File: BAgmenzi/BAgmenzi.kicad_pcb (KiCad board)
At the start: 6 copper layers, 140 parts, among them IC1 TPL0501-100RSER, J2 DF52-2S-0.8H(21), J3 USB3076-30-A, M1 *, Q1 NX7002BKMBYL, U1 MSP430FR5043IRGCT, U10 PESD1USB30, U11 MAX77654BENV+T, U12 TS5A3159AYZPR, U13 TPS7A2033DBVDQN, U14 TPS63900, U2 AD8338ACPZ-R7, U3 OPA836IDBVT, U4 OPA836IDBVT, U7 LT3463AEDD#PBF, U8 TPS22916CYFPR, U9 MAXM86161EFD_T, X1 FY0800018, X2 ABS07-32.768KHZ-9-T, Y1 AWSCR-8.00CV-T

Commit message: started layout, front v backside
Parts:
- removed C55: 0.1u, Capacitor_SMD:C_0402_1005Metric
- removed C56: 10u, Capacitor_SMD:C_0402_1005Metric
- removed C57: 22u, Capacitor_SMD:C_0402_1005Metric
- removed D1: APHD1608LZGCK, wulpus:FP-APHD1608LZGCK-MFG
- removed L8: 2.2uH, Inductor_SMD:L_Murata_DFE201610P
- removed R37: 100k, Resistor_SMD:R_0402_1005Metric
- removed R38: 20.5k, Resistor_SMD:R_0402_1005Metric
- removed R39, R40: 0, Resistor_SMD:R_0402_1005Metric
- removed R6: 22, Resistor_SMD:R_0402_1005Metric
- removed U12: TS5A3159AYZPR, wulpus_pro_acq:BGA6C50P2X3_89X139X50
- removed U14: TPS63900, Package_SON:WSON-10-1EP_2.5x2.5mm_P0.5mm_EP1.2x2mm_ThermalVias
- added C61: 2.2U 50v, EEG_PcbLib:0402, F.Cu at (149.6, 117.5)
- added C62: 2.2U 50v, EEG_PcbLib:0402, F.Cu at (165.4, 141.2)
- added J1: Conn_01x07, Connector_PinHeader_2.54mm:PinHeader_1x07_P2.54mm_Vertical, F.Cu at (74.3, 168.0)
- added J4: connector for CMUT, cmut_dummy:cmut-dummy, F.Cu at (159.9, 128.7)
- added J5: 3220-10-0100-00, EEG_PcbLib:CONN_3220-10-0100-00_CNC, F.Cu at (35.2, 166.0)
- added JP1: SolderJumper_3_Open, Jumper:SolderJumper-3_P1.3mm_Open_Pad1.0x1.5mm, F.Cu at (146.7, 141.7)
- added JP2: SolderJumper_3_Open, Jumper:SolderJumper-3_P1.3mm_Open_Pad1.0x1.5mm, F.Cu at (149.4, 110.5)
- added JP3: SolderJumper_3_Open, Jumper:SolderJumper-3_P1.3mm_Open_Pad1.0x1.5mm, F.Cu at (146.7, 137.9)
- added JP4: SolderJumper_3_Open, Jumper:SolderJumper-3_P1.3mm_Open_Pad1.0x1.5mm, F.Cu at (149.4, 115.2)
- added JP5: SolderJumper_3_Open, Jumper:SolderJumper-3_P1.3mm_Open_Pad1.0x1.5mm, F.Cu at (165.1, 138.7)
- added JP7: SolderJumper_3_Open, Jumper:SolderJumper-3_P1.3mm_Open_Pad1.0x1.5mm, F.Cu at (37.4, 112.6)
- added R41: 100K, Resistor_SMD:R_0402_1005Metric, F.Cu at (150.0, 112.3)
- added R42: 100K, Resistor_SMD:R_0402_1005Metric, F.Cu at (146.6, 135.4)
- added R43: 100K, EEG_PcbLib:0402, F.Cu at (149.6, 118.7)
- added R44: 30k, EEG_PcbLib:0402, F.Cu at (163.6, 141.0)
- C33: footprint Capacitor_SMD:C_0201_0603Metric -> Capacitor_SMD:C_0402_1005Metric
- C59: value 1u -> 2.2u
- C63: footprint Capacitor_SMD:C_0201_0603Metric -> EEG_PcbLib:0402
- TP2: footprint TestPoint:TestPoint_Loop_D2.50mm_Drill1.85mm -> TestPoint:TestPoint_Pad_D2.0mm
- TP6: footprint TestPoint:TestPoint_Loop_D2.50mm_Drill1.0mm_LowProfile -> TestPoint:TestPoint_Pad_D2.0mm
- TP7: footprint EEG_PcbLib:TEST_POINT_KEYSTONE_5007_TRAD -> TestPoint:TestPoint_THTPad_1.0x1.0mm_Drill0.5mm
- moved L6 220.9 mm to (41.8, 140.3)
- moved R21 220.0 mm to (46.0, 137.1)
- moved R22 220.0 mm to (48.5, 139.9)
- moved R25 220.0 mm to (44.9, 142.3)
- moved C39 220.0 mm to (41.7, 139.2)
- moved C40 220.0 mm to (44.3, 137.2)
- moved C43 220.0 mm to (50.0, 141.4)
- moved D2 220.0 mm to (47.5, 142.4)
- moved L5 220.0 mm to (42.6, 138.1)
- moved R20 220.0 mm to (46.0, 136.1)
- moved R23 220.0 mm to (48.5, 140.9)
- moved R24 220.0 mm to (43.8, 142.3)
- moved U7 220.0 mm to (45.6, 139.3)
- moved C41 219.8 mm to (45.7, 134.7)
- moved C42 219.8 mm to (45.7, 133.5)
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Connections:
- net /POWER/V_RX_3.6V renamed Net-(JP7-C)
- net soft_RST renamed nRST
- U1 pad 45: /MSP/TRIG_OUT -> unconnected-(U1-P6.6_ACLK-Pad45)
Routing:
- net /TX/PULSER_OUT: track 11.0 -> 1.26 mm
- net /RX/VGA_IN: track 5.69 -> 0.00 mm, vias 1 -> 0
- net +HV: track 7.05 -> 1.37 mm
- net GND: track 11.0 -> 6.09 mm, vias 18 -> 12
- net Net-(U3-VIN-): track 3.27 -> 0.00 mm
- net Net-(U3-VIN+): track 2.30 -> 0.00 mm
- net Net-(C28-Pad2): track 1.22 -> 0.00 mm
- net (no net): track 1.07 -> 0.00 mm
- net V_RX: track 1.06 -> 0.00 mm
- net Net-(C25-Pad2): track 1.04 -> 0.00 mm
- net /RX/VGA_REF: track 1.01 -> 0.00 mm
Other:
- board text added: "BACKSIDE"
- board text added: "GND"
- board text added: "RST"
- board text added: "RX"
- board text added: "TEST"
- board text added: "TX"
- board text added: "VDD"
- board text added: "fRONTSIDE: skin"

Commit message: small changes
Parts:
- C10, C11, C12, C2, C3, C32, C33, C37, C38, C39, C4, C40, C41, C42, C43, C44, C45, C46, C47, C48, C49, C5, C50, C51, C52, C53, C54, C58, C59, C6, C60, C64, C65, C7, C8, C9, D2, D4, FB1, FB2, FB3, J1, J2, J3, J5, JP6, JP7, L1, L2, L5, L6, L7, M1, R1, R14, R20, R21, R22, R23, R24, R25, R32, R33, R34, R35, R36, RT1, S1, TP2, TP6, TP7, U10, U11, U13, U7, U8: moved to B.Cu
- moved C45 138.4 mm to (166.7, 107.7)
- moved C44 134.5 mm to (164.1, 105.6), turned to 0 degrees
- moved J5 132.9 mm to (165.9, 141.9), turned to 180 degrees
- moved C46 131.2 mm to (161.8, 108.0)
- moved JP7 130.2 mm to (165.9, 91.7)
- moved U13 124.0 mm to (162.8, 91.6)
- moved C58 123.8 mm to (162.7, 90.1), turned to 180 degrees
- moved C59 123.7 mm to (162.6, 93.3), turned to 180 degrees
- moved C39 121.8 mm to (161.6, 118.4), turned to 0 degrees
- moved FB3 121.7 mm to (161.6, 95.0), turned to 180 degrees
- moved L6 121.5 mm to (161.5, 119.5), turned to 180 degrees
- moved C33 120.6 mm to (161.0, 121.1)
- moved C60 120.3 mm to (160.9, 96.9), turned to 0 degrees
- moved L5 120.0 mm to (160.7, 117.3), turned to 180 degrees
- moved R24 117.5 mm to (159.5, 121.5)
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
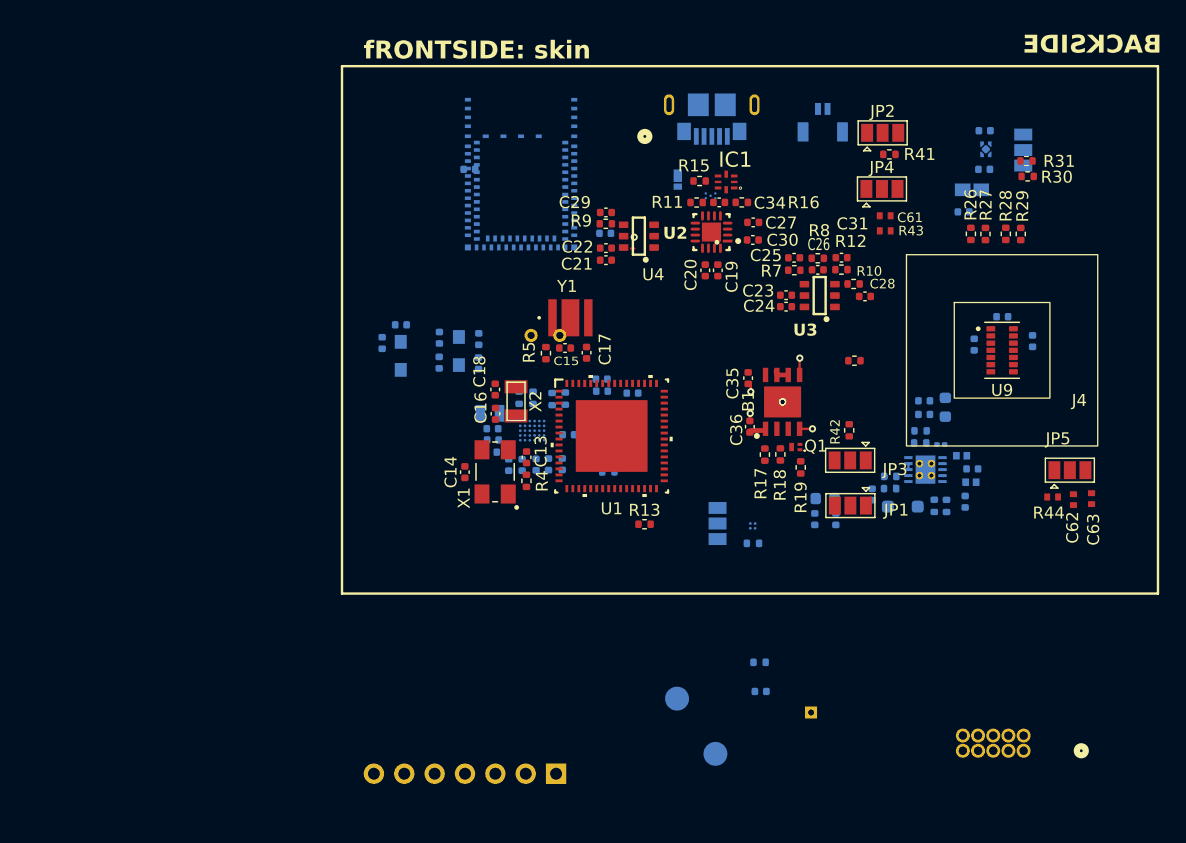
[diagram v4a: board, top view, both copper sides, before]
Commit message: started routing, changed enable signals to nRF
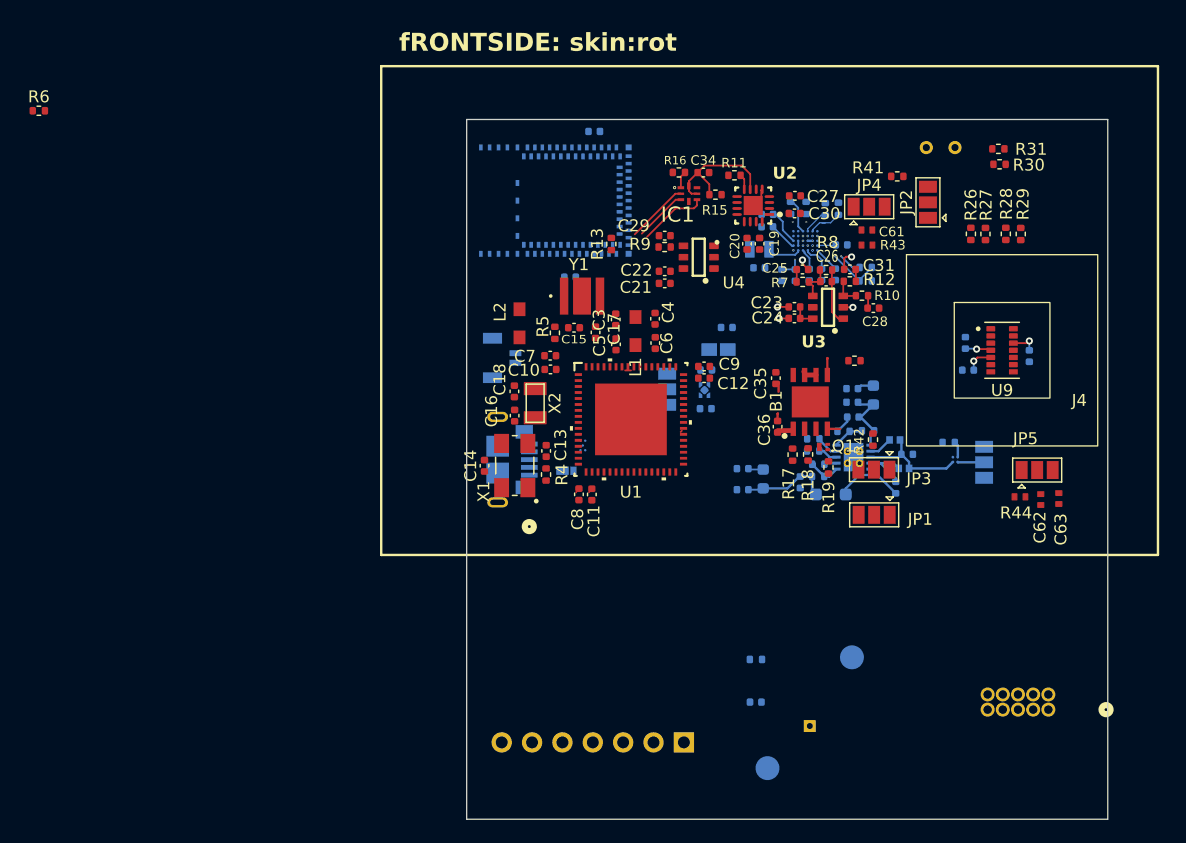
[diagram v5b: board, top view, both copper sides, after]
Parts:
- added R6: 100k, Resistor_SMD:R_0402_1005Metric, F.Cu at (83.5, 88.4)
- C10, C11, C12, C3, C4, C5, C6, C7, C8, C9, L1, L2: moved to F.Cu
- C40: footprint Capacitor_SMD:C_0201_0603Metric -> Capacitor_SMD:C_0402_1005Metric
- moved JP7 35.9 mm to (136.1, 111.7), turned to 90 degrees
- moved J3 34.6 mm to (121.9, 117.6), turned to 90 degrees
- moved S1 34.5 mm to (157.8, 91.5), turned to 0 degrees
- moved J2 33.2 mm to (122.5, 109.1), turned to 90 degrees
- moved C58 32.9 mm to (139.3, 113.3), turned to 0 degrees
- moved U13 31.0 mm to (139.2, 111.8), turned to -90 degrees
- moved C49 29.7 mm to (144.5, 97.1)
- moved C59 28.7 mm to (139.4, 110.1), turned to 0 degrees
- moved C53 28.5 mm to (144.5, 98.1)
- moved U11 27.8 mm to (148.7, 98.5)
- moved C48 27.8 mm to (149.0, 102.1)
- moved R35 27.8 mm to (150.4, 96.6)
- moved C50 27.8 mm to (150.2, 102.1)
- moved C52 27.8 mm to (148.0, 102.1)
- moved R33 27.8 mm to (149.3, 96.6)
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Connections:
- M1 pad 72: unconnected-(M1-P1.17-Pad72) -> HV_NEG_EN
- M1 pad 73: unconnected-(M1-P1.16-Pad73) -> HV_POS_EN
- M1 pad 74: unconnected-(M1-P1.15-Pad74) -> HV_PWR_EN
- M1 pad 75: unconnected-(M1-P1.14-Pad75) -> VRX_EN
- U1 pad 20: VRX_EN -> unconnected-(U1-P1.3_UCA1SOMI_UCA1RXD_TA1.1_A9_C9-Pad20)
- U1 pad 38: /MSP/VGA_SPI.CLK -> VGA_SPI.SCLK
- U1 pad 50: HV_POS_EN -> unconnected-(U1-P3.3_MCLK_TB0.3_XPB1-Pad50)
- U1 pad 51: HV_NEG_EN -> unconnected-(U1-P3.4_SMCLK_DMAE0-Pad51)
- U1 pad 52: HV_PWR_EN -> unconnected-(U1-P3.5_ACLK_COUT-Pad52)
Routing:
- net /RX/VGA_GAIN: track 0.00 -> 11.1 mm
- net /TX/+V_IN_HV: track 0.22 -> 9.24 mm
- net GND: track 6.09 -> 15.0 mm
- net /TX/VOUT_NEG: track 0.00 -> 7.43 mm
- net Net-(U11A-THM): track 0.00 -> 6.72 mm, vias 0 -> 2
- net V_LED: track 0.00 -> 6.44 mm, vias 0 -> 3
- net Net-(D2-K): track 0.00 -> 6.34 mm
- net /TX/VOUT_POS: track 0.04 -> 6.13 mm
- net VGA_SPI.SCLK: track 0.00 -> 5.74 mm
- net Net-(U11A-TBIAS): track 0.00 -> 5.51 mm, vias 0 -> 2
- net VGA_SPI.MOSI: track 0.00 -> 5.41 mm
- net Net-(U7-SW2): track 0.07 -> 5.45 mm
- net /RX/VGA_IN: track 0.00 -> 4.71 mm
- net VGA_GAIN_CS: track 0.00 -> 4.44 mm
- net /POWER/PMIC_EN: track 0.00 -> 4.41 mm, vias 0 -> 2
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- added copper zone on In1.Cu, net GND
- added copper zone on In4.Cu, net GND
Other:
- board outline added: 53.6 x 58.5 mm
- board text added: "BACKSIDE: blau"
- board text added: "fRONTSIDE: skin:rot"
- board text removed: "BACKSIDE"
- board text removed: "fRONTSIDE: skin"

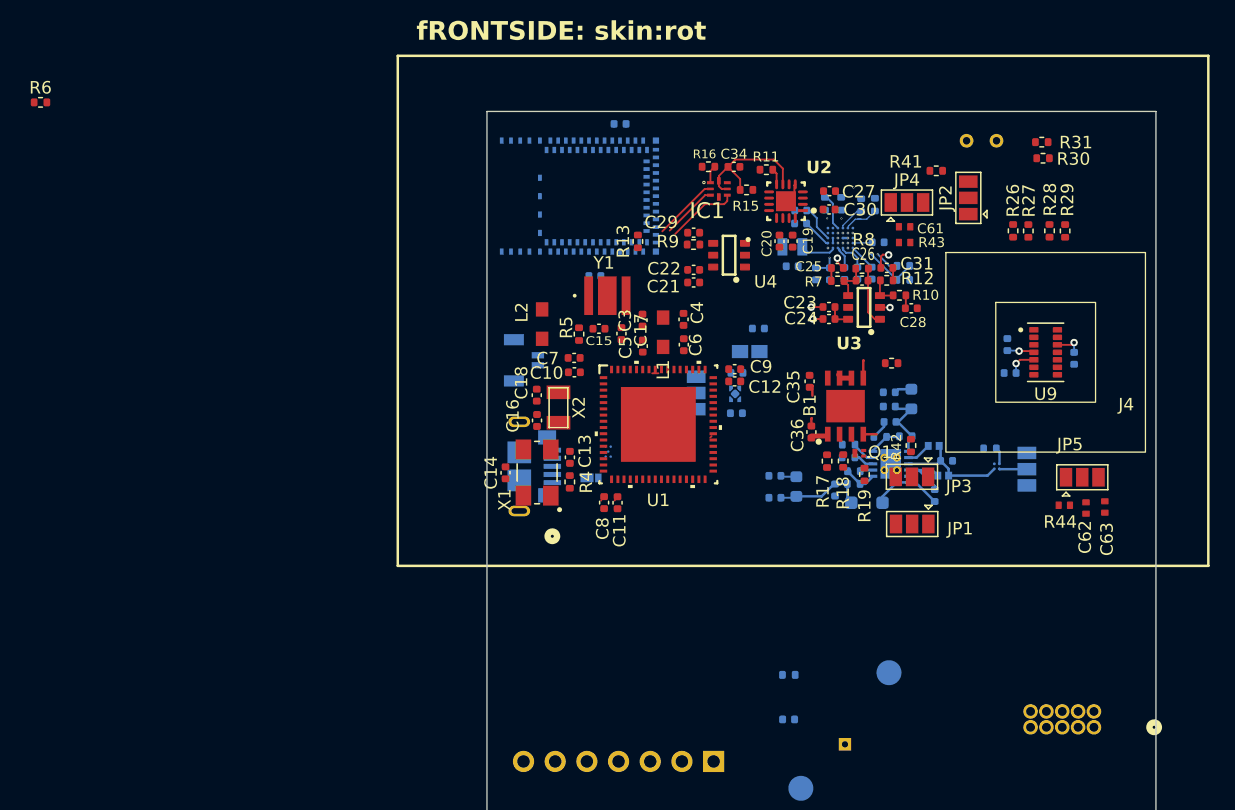
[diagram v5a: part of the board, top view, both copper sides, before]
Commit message: routed msp and nrf
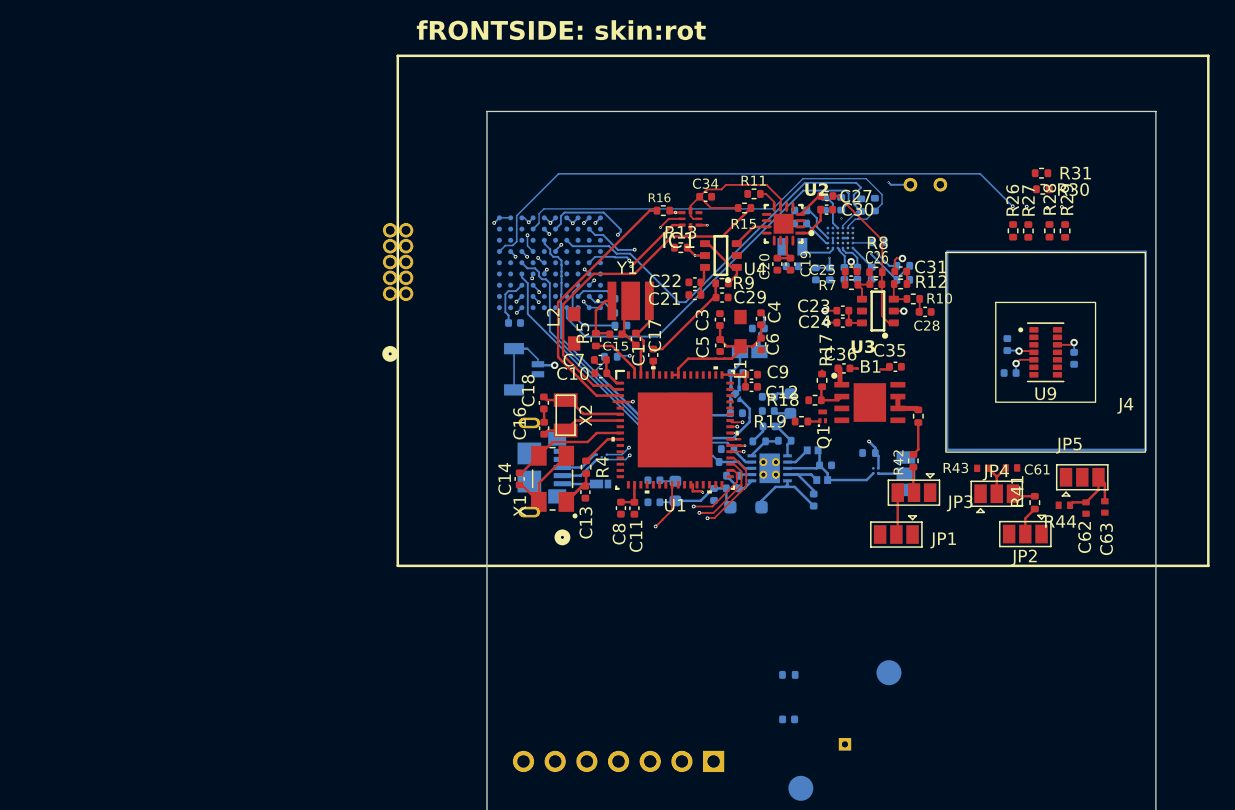
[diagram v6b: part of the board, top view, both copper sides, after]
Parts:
- added C1: 1n, Capacitor_SMD:C_0402_1005Metric, F.Cu at (132.7, 108.7)
- added C55: 100n, Capacitor_SMD:C_0402_1005Metric, B.Cu at (130.1, 104.1)
- added C66: 100n, Capacitor_SMD:C_0402_1005Metric, B.Cu at (130.1, 106.3)
- M1: value * -> ~; footprint AN54LM-20_PCB-260723:AN54LM-20_P20 -> nRFPCB:BM20-C
- R6: moved to B.Cu
- moved J5 66.3 mm to (111.6, 103.7), turned to 90 degrees
- moved R6 50.1 mm to (129.3, 108.8)
- moved R41 27.7 mm to (163.2, 120.5), turned to 90 degrees
- moved JP2 27.3 mm to (162.5, 123.0), turned to 180 degrees
- moved JP4 24.4 mm to (160.2, 119.8)
- moved C61 21.1 mm to (161.4, 117.7)
- moved R43 19.2 mm to (159.1, 117.7), turned to 180 degrees
- moved C65 18.1 mm to (121.5, 106.1)
- moved R25 10.9 mm to (137.4, 117.2)
- moved C39 9.71 mm to (146.5, 117.5)
- moved C40 9.71 mm to (141.9, 114.4)
- moved C41 9.71 mm to (141.9, 113.1)
- moved C42 9.71 mm to (141.9, 112.0)
- moved JP6 9.71 mm to (152.9, 118.2)
- moved L5 9.71 mm to (145.4, 116.3)
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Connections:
- R17 pad 1: PULSE_OUT -> unconnected-(R17-Pad1)
- R17 pad 2: /TX/PULSER_IN -> unconnected-(R17-Pad2)
- U1 pad 29: /MSP/LED_MSP430 -> unconnected-(U1-P4.1_UCA0CLK_TB0.4_UCA3SOMI_UCA3RXD-Pad29)
- U3 pad 5: VRX_EN -> V_RX
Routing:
- net PPG_I2C.SDA: track 0.00 -> 67.3 mm, vias 0 -> 2
- net PMIC_AMUX: track 0.00 -> 62.9 mm, vias 0 -> 2
- net PPG_INT: track 0.00 -> 54.6 mm, vias 0 -> 2
- net PPG_I2C.SCL: track 0.00 -> 46.3 mm, vias 0 -> 2
- net PPG_GPIO: track 0.00 -> 46.0 mm, vias 0 -> 1
- net HV_PWR_EN: track 1.32 -> 39.6 mm, vias 0 -> 2
- net NRF_SPI.MOSI: track 0.00 -> 37.1 mm, vias 0 -> 2
- net NRF_SPI.SCLK: track 0.00 -> 35.6 mm, vias 0 -> 2
- net NRF_MSP_CS: track 0.00 -> 35.2 mm, vias 0 -> 2
- net NRF_SPI.MISO: track 0.00 -> 33.2 mm, vias 0 -> 2
- net PMIC_I2C.SDA: track 2.14 -> 34.3 mm
- net nRST: track 3.32 -> 35.5 mm
- net VRX_EN: track 0.00 -> 31.7 mm
- net DATA_READY: track 0.00 -> 31.6 mm, vias 0 -> 2
- net UUPS_TRIG_IN: track 0.00 -> 30.6 mm, vias 0 -> 2
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
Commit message: powerplanes
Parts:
- removed TP2: vga_vref, TestPoint:TestPoint_Pad_D2.0mm
- removed TP6: TestPoint, TestPoint:TestPoint_Pad_D2.0mm
- removed TP7: +V_hv_in, TestPoint:TestPoint_THTPad_1.0x1.0mm_Drill0.5mm
- added R45: 220, EEG_PcbLib:0402, B.Cu at (116.7, 104.9)
- added R46: 220, EEG_PcbLib:0402, B.Cu at (116.7, 103.5)
- J5: footprint EEG_PcbLib:CONN_3220-10-0100-00_CNC -> Connector_PinHeader_1.27mm:PinHeader_2x05_P1.27mm_Vertical_SMD
- R26, R27, R28, R29, R30, R31: moved to B.Cu
- moved R30 28.3 mm to (164.9, 123.7), turned to 180 degrees
- moved R31 26.3 mm to (163.2, 120.4), turned to 180 degrees
- moved R26 26.0 mm to (167.5, 124.0), turned to 180 degrees
- moved R28 24.4 mm to (167.5, 122.9), turned to 180 degrees
- moved R29 23.7 mm to (164.9, 122.4), turned to 180 degrees
- moved R27 23.6 mm to (167.4, 121.9), turned to 180 degrees
- moved C2 11.5 mm to (133.3, 132.4)
- moved J1 11.3 mm to (139.0, 130.1)
- moved R1 8.31 mm to (135.4, 132.4)
- moved C30 4.63 mm to (145.3, 101.4), turned to 90 degrees
- moved S1 1.65 mm to (155.8, 96.7)
- moved J5 1.44 mm to (111.9, 102.3), turned to 0 degrees
- moved C27 1.21 mm to (146.3, 97.1)
- moved C3 1.17 mm to (137.8, 107.0), turned to 180 degrees
- moved C28 1.01 mm to (154.0, 106.1), turned to 90 degrees
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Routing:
- net PPG_I2C.SCL: track 46.3 -> 93.4 mm
- net GND: track 43.8 -> 89.8 mm, vias 23 -> 67
- net DVDD_3.3: track 20.5 -> 56.1 mm, vias 1 -> 13
- net JTAG.TEST: track 0.00 -> 33.1 mm
- net SPARE_PIN: track 0.00 -> 30.1 mm, vias 0 -> 1
- net JTAG.RESET_N: track 0.00 -> 29.6 mm
- net PPG_INT: track 54.6 -> 81.1 mm
- net /RX/VGA_REF: track 1.01 -> 23.8 mm, vias 0 -> 2
- net SWDIO: track 0.00 -> 20.5 mm
- net PPG_GPIO: track 46.0 -> 66.0 mm, vias 1 -> 0
- net Net-(U9-GPIO): track 0.00 -> 18.4 mm, vias 0 -> 1
- net BSL.UART_RX: track 0.00 -> 17.2 mm
- net +HV: track 2.76 -> 16.4 mm, vias 0 -> 4
- net PPG_I2C.SDA: track 67.3 -> 80.1 mm
- net BSL.UART_TX: track 0.00 -> 12.6 mm
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- added copper zone on In1.Cu, net (none)
- added copper zone on In4.Cu, net (none)
- added copper zone on In2.Cu, net +HV
- added copper zone on In2.Cu, net -HV
- added copper zone on In3.Cu, net DVDD_3.3
- added copper zone on In2.Cu, net V_BAT
- added copper zone on In2.Cu, net V_LED
- added copper zone on In2.Cu, net V_RX
- added copper zone on In2.Cu, net V_SYS
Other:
- board size 53.6 x 58.5 mm -> 66.2 x 44.8 mm
